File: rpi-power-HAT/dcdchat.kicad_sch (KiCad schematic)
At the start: 29 parts

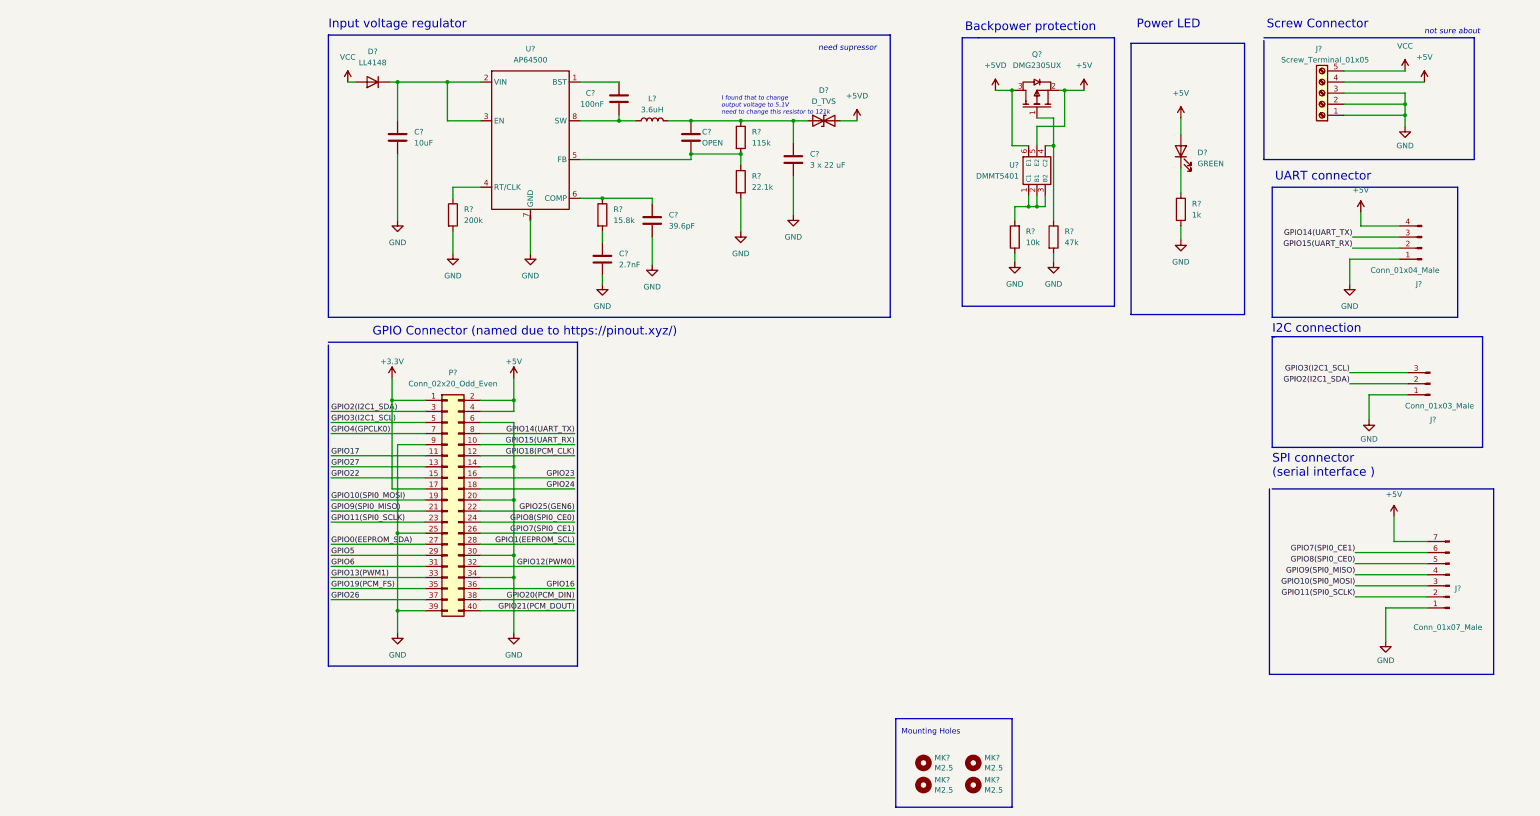
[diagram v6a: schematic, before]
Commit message: fixed 2, 3, 4, 5, 6 in 25.11.2024 message
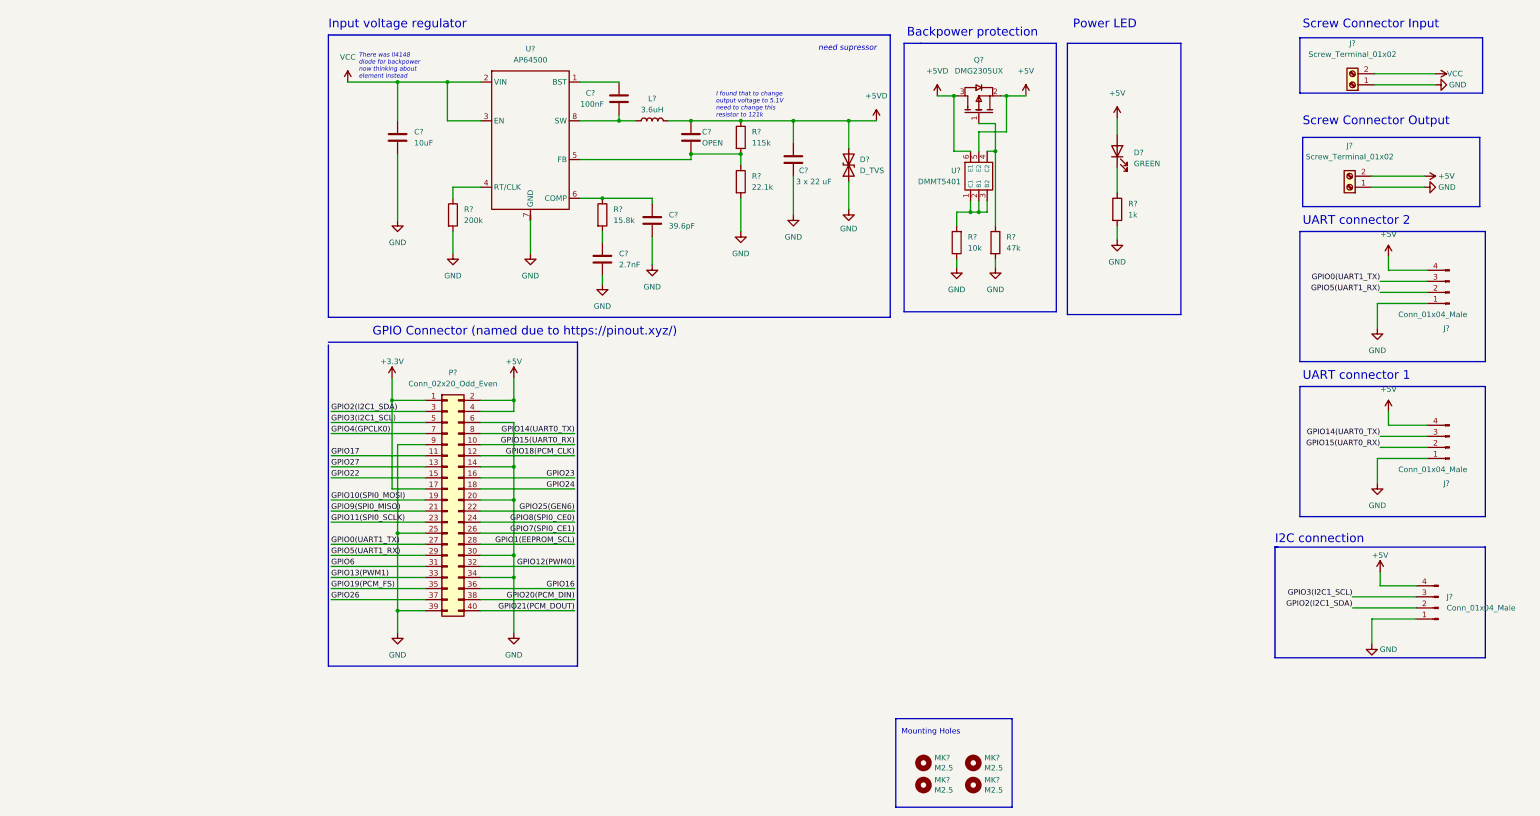
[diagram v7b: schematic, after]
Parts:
- removed D?: LL4148, Diode_SMD:D_MiniMELF, symbol Diode:LL4148
- removed D?: D_TVS, symbol Device:D_TVS
- removed J?: Conn_01x07_Male, symbol Connector:Conn_01x07_Male
- removed J?: Screw_Terminal_01x05, symbol Connector:Screw_Terminal_01x05
- removed J?: Conn_01x03_Male, symbol Connector:Conn_01x03_Male
- added D?: D_TVS, symbol Device:D_TVS
- added J? (x2): Screw_Terminal_01x02, symbol Connector:Screw_Terminal_01x02
- added J? (x2): Conn_01x04_Male, symbol Connector:Conn_01x04_Male
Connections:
- net +5V: now also J?.2 (Pin_2), J?.4 (Pin_4), J?.4 (Pin_4)
- net +5VD: now also C?.1, C?.1, L?.2, R?.1, D?.2 (A2)
- net GND: now also D?.1 (A1), J?.1 (Pin_1), J?.1 (Pin_1), J?.1 (Pin_1), J?.1 (Pin_1)
- net GPIO2(I2C1_SDA): now also J?.2 (Pin_2)
- net GPIO3(I2C1_SCL): now also J?.3 (Pin_3)
- net VCC: now also C?.1, U?.2 (VIN), U?.3 (EN), J?.2 (Pin_2)
- net GPIO0(EEPROM_SDA) renamed GPIO0(UART1_TX)
- net GPIO0(UART1_TX): now also J?.3 (Pin_3)
- net GPIO14(UART_TX) renamed GPIO14(UART0_TX)
- net GPIO15(UART_RX) renamed GPIO15(UART0_RX)
- net GPIO5 renamed GPIO5(UART1_RX)
- net GPIO5(UART1_RX): now also J?.2 (Pin_2)
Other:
- note added: "Screw Connector Input"
- note added: "Screw Connector Output"
- note added: "There was ll4148 diode for backpower now thinking about element instead"
- note added: "UART connector 1"
- note added: "UART connector 2"
- note removed: "SPI connector (serial interface )"
- note removed: "Screw Connector"
- note removed: "UART connector"
- note removed: "not sure about"
- moved on the sheet: D?, J?, Q?, R?, U?

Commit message: fixed 7, 8. Added level converter from 5v to 3.3V
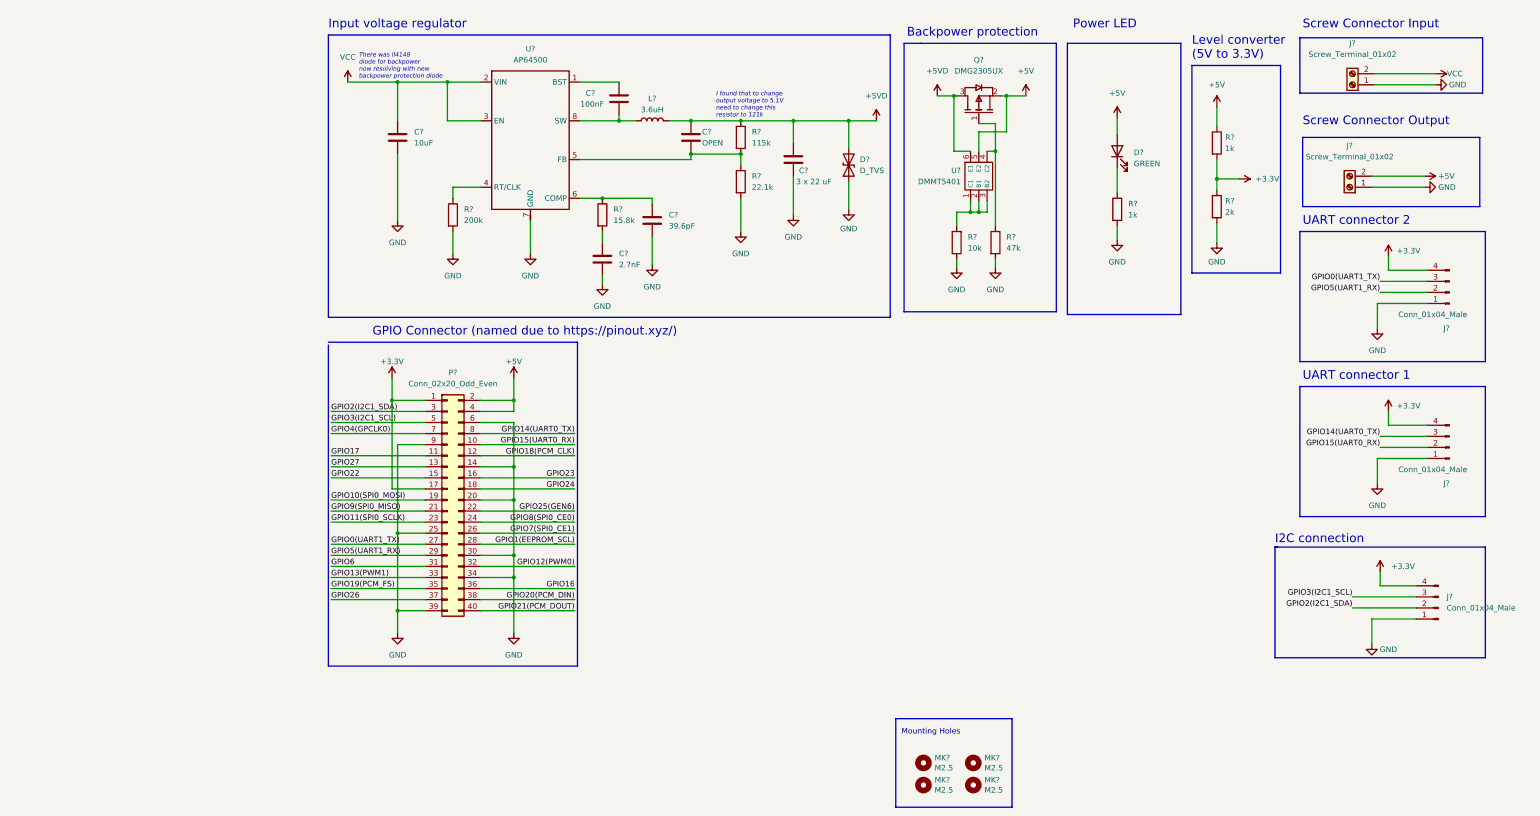
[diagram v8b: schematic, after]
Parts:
- added R?: 2k, symbol Device:R
- added R?: 1k, symbol Device:R
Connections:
- net +3.3V: now also J?.4 (Pin_4), J?.4 (Pin_4), J?.4 (Pin_4), R?.1, R?.2
- net +5V: now also R?.1; no longer J?.4 (Pin_4), J?.4 (Pin_4), J?.4 (Pin_4)
- net GND: now also R?.2
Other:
- note added: "Level converter (5V to 3.3V)"
- note added: "There was ll4148 diode for backpower now resolving with new backpower protection diode"
- note removed: "There was ll4148 diode for backpower now thinking about element instead"
- note removed: "need supressor"
